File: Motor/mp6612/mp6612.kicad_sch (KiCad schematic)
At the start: 32 parts, among them J1 Conn_01x07, J2 OQ0212500000G, J3 TB002-500-02BE, U1 MP6612DGF-P

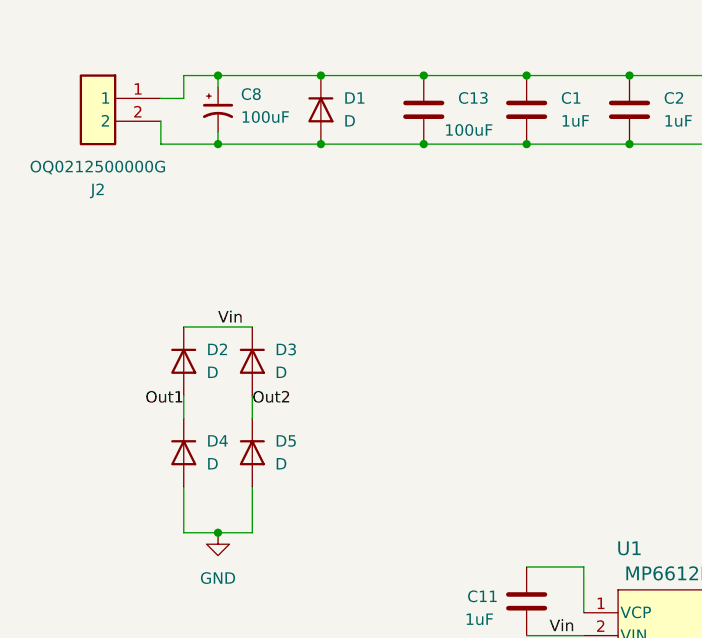
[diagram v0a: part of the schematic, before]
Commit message: Rename Project
Rename project to MP6612
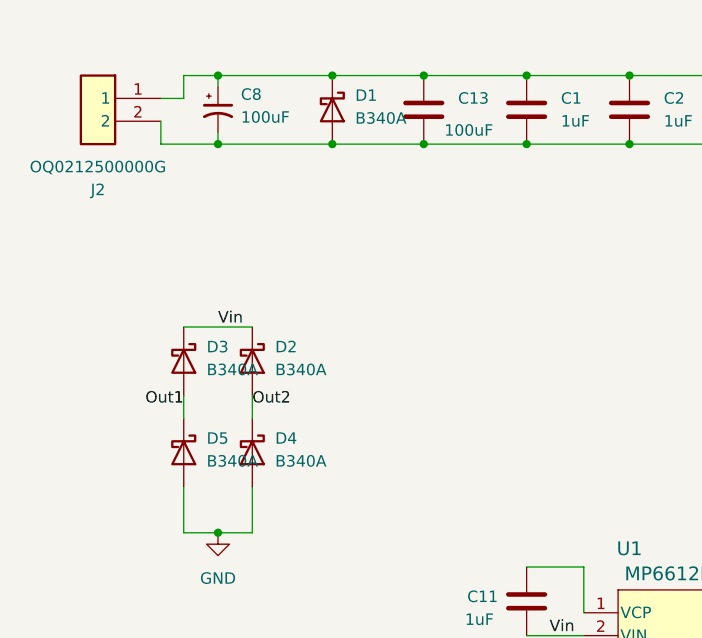
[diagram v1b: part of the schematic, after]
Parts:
- removed D1, D2, D3, D4, D5: D, Diode_SMD:D_1206_3216Metric, symbol Device:D
- added D1, D2, D3, D4, D5: B340A, Diode_SMD:D_SMA, symbol _Misc_Symbols:B340A
- RV1: footprint Potentiometer_SMD:Potentiometer_ACP_CA6-VSMD_Vertical -> Potentiometer_THT:Potentiometer_Runtron_RM-065_Vertical
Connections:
- net GND: now also D1.2 (A), D4.2 (A), D5.2 (A)
- net Out1: now also D3.2 (A), D5.1 (K)
- net Out2: now also D2.2 (A), D4.1 (K)
- net Vin: now also D1.1 (K), D2.1 (K), D3.1 (K)
